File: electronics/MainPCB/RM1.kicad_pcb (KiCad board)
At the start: 2 copper layers, 113 x 76 mm, 33 parts, among them J1 AVR-ISP-6, J10 Conn_01x02, J2 Conn_01x08, J3 Conn_01x06, J4 Conn_01x08, J5 Conn_01x06, J6 Conn_01x02, J7 Conn_01x07, J8 Conn_01x03, J9 Conn_01x02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

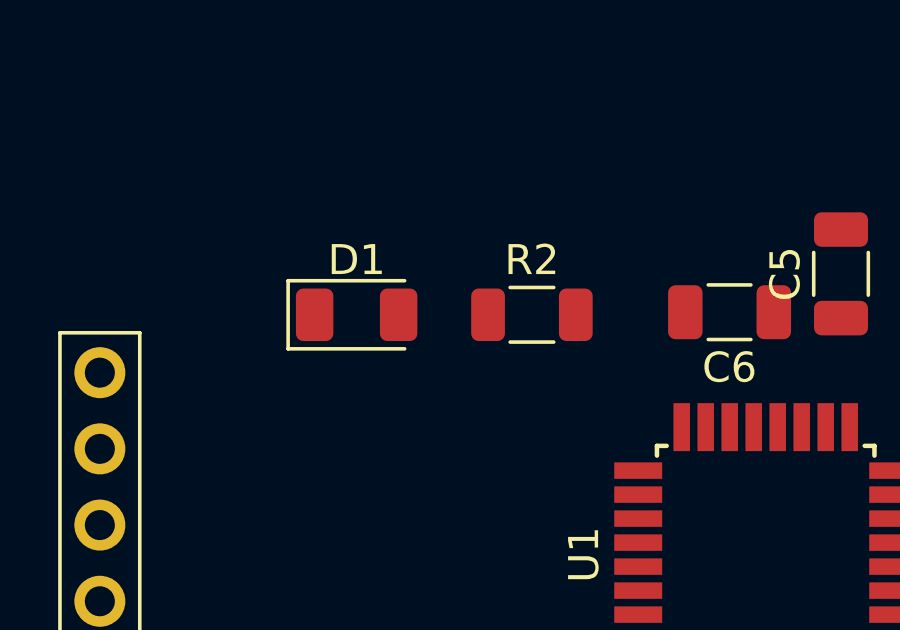
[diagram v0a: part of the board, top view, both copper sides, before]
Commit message: initiated project of electronics in smd
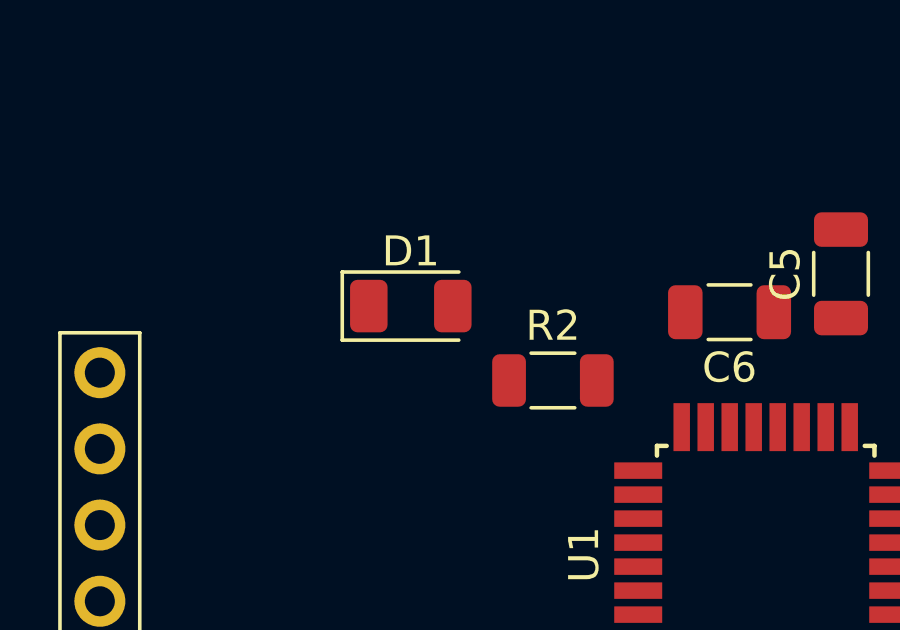
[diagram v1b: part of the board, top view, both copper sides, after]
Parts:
- moved R2 2.30 mm to (74.3, 71.2)
- moved D1 1.83 mm to (69.6, 68.7)
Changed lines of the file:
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@@
   )
   (footprint "LED_SMD:LED_1206_3216Metric" (layer "F.Cu")
-    (at 67.765 69.01)
+    (at 69.57 68.72)
     (descr "LED SMD 1206 (3216 Metric), square (rectangular) end terminal, IPC_7351 nominal, (Body size source: http://www.tortai-tech.com/upload/download/2011102023233369053.pdf), generated with kicad-footprint-generator")
     (tags "LED")
@@
   )
   (footprint "Resistor_SMD:R_1206_3216Metric" (layer "F.Cu")
-    (at 73.6075 69.01)
+    (at 74.3075 71.2)
     (descr "Resistor SMD 1206 (3216 Metric), square (rectangular) end terminal, IPC_7351 nominal, (Body size source: IPC-SM-782 page 72, https://www.pcb-3d.com/wordpress/wp-content/uploads/ipc-sm-782a_amendment_1_and_2.pdf), generated with kicad-footprint-generator")
     (tags "resistor")
@@
     )
   )
+  (group "" (id 4d3fc5d5-c848-44a8-bc55-1bd5917979f2)
+    (members
+      00000000-0000-0000-0000-000060ad8b8e
+      00000000-0000-0000-0000-000060ad8d5c
+    )
+  )
   (group "" (id 57b01d0f-84b1-4988-8f8b-32f5c4b93a5f)
     (members
@@
     )
   )
-  (group "" (id bc05f071-bbf3-43e5-b1f5-9627021724bf)
-    (members
-      00000000-0000-0000-0000-000060ad8b8e
-      00000000-0000-0000-0000-000060ad8d5c
-    )
-  )
